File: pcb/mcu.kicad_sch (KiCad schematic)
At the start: 34 parts, among them J1 XF2M-1415-1A, SW1 EVQ-Q2B02W, SW2 EVQ-Q2B02W, U1 ESP32-S3-WROOM-1-N8R2

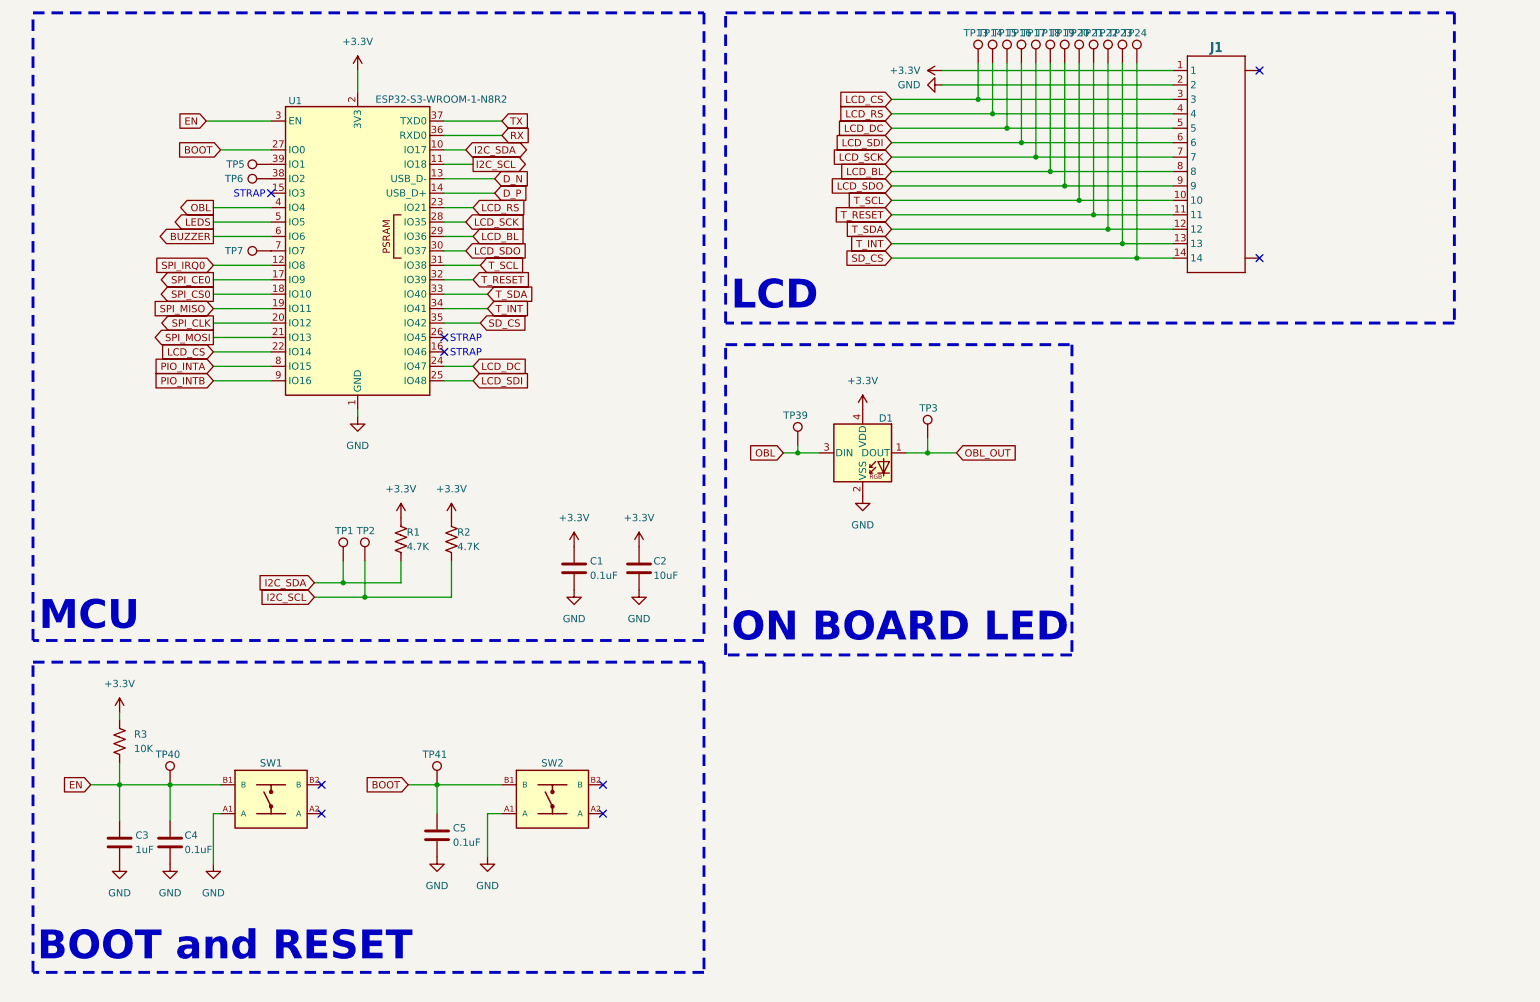
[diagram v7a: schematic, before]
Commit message: Sync symbols and footprints
Transitioned to CRGM footprints
Added dimensions
Fixed some spacing
Adjusted properties
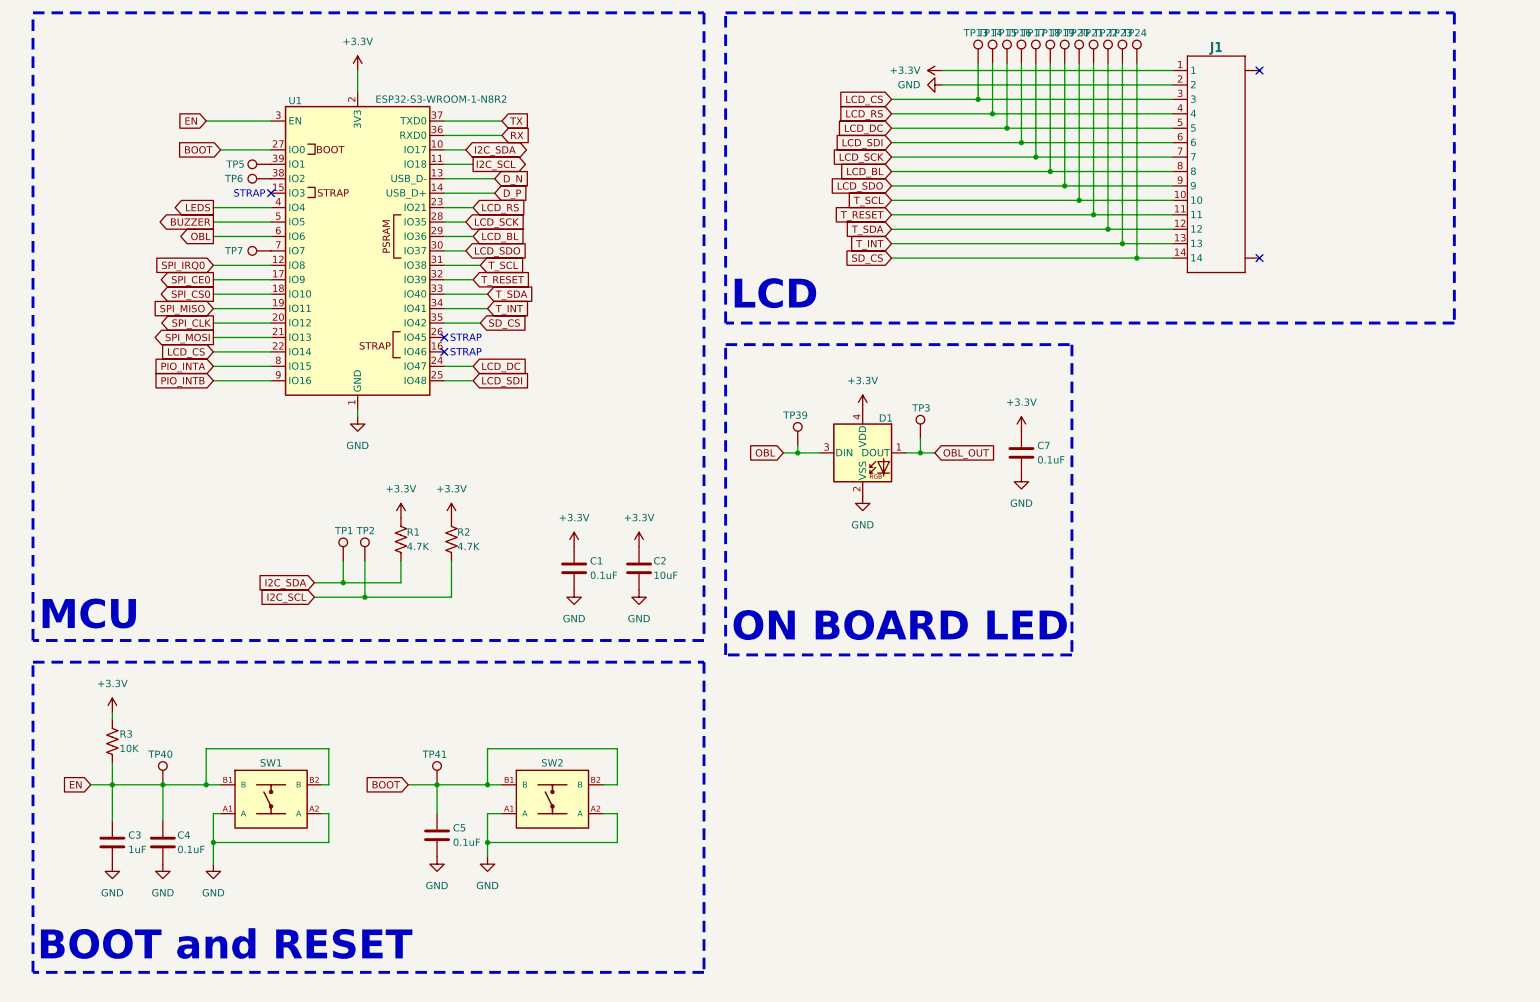
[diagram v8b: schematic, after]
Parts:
- added C7: 0.1uF, CRGM Passive:C_0603_1608Metric, symbol Device:C
- C1, C2, C3, C4, C5: footprint Capacitor_SMD:C_0603_1608Metric -> CRGM Passive:C_0603_1608Metric
- D1: footprint LED_SMD:LED_WS2812B-2020_PLCC4_2.0x2.0mm -> CRGM Passive:LED_WS2812B-2020_PLCC4_2.0x2.0mm
- R1, R2, R3: footprint Resistor_SMD:R_0603_1608Metric -> CRGM Passive:R_0603_1608Metric
- U1: MN Espressif Systems -> (none); MPN ESP32-S3-WROOM-1-N8R2 -> (none)
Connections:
- net +3.3V: now also C7.1
- net BOOT: now also SW2.B2 (B)
- net BUZZER: now also U1.5 (IO5); no longer U1.6 (IO6)
- net EN: now also SW1.B2 (B)
- net GND: now also SW1.A2 (A), SW2.A2 (A), C7.2
- net LEDS: now also U1.4 (IO4); no longer U1.5 (IO5)
- net OBL: now also U1.6 (IO6); no longer U1.4 (IO4)
- no-connect marks 9 -> 5
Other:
- moved on the sheet: C3, C4, R3, TP3, TP40
